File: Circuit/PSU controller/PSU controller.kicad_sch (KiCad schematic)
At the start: 13 parts, among them Q1 S8050

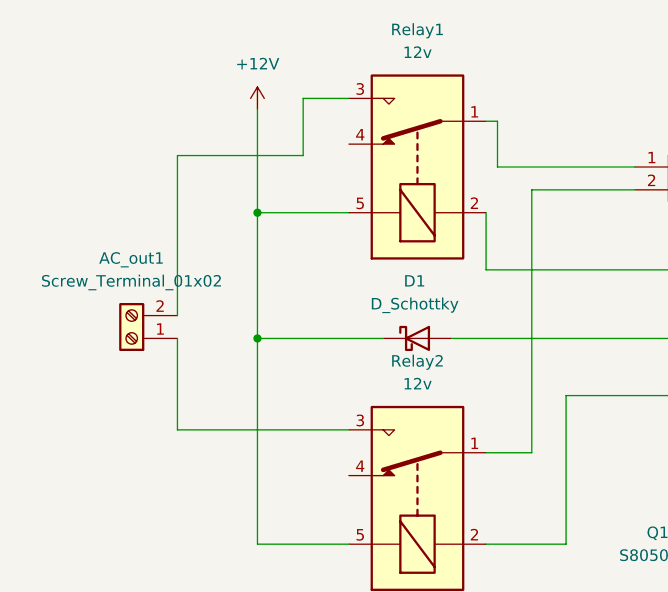
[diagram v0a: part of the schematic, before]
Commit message: Modified PSU controller circuit
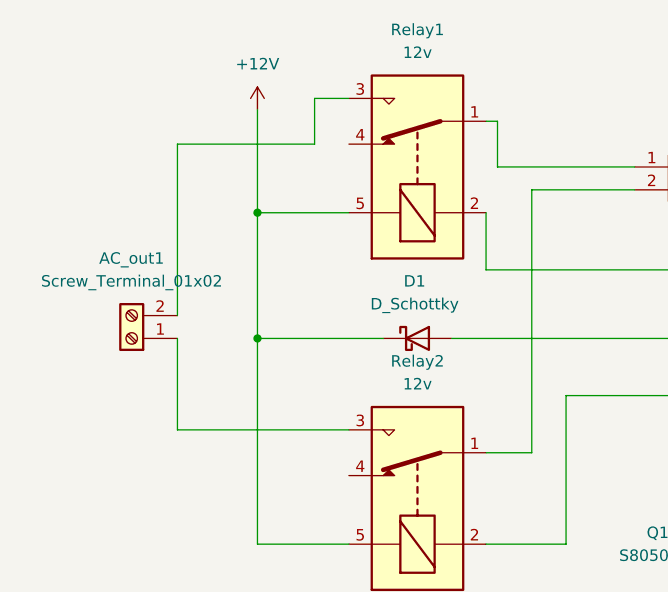
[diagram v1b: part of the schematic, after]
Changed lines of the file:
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@@
+    (stroke (width 0) (type default) (color 0 0 0 0))
+  )
+  (wire (pts (xy 147.32 41.91) (xy 162.56 41.91))
     (stroke (width 0) (type default) (color 0 0 0 0))
   )
@@
     (stroke (width 0) (type default) (color 0 0 0 0))
   )
+  (wire (pts (xy 162.56 36.83) (xy 166.37 36.83))
+    (stroke (width 0) (type default) (color 0 0 0 0))
+  )
   (wire (pts (xy 255.27 74.93) (xy 261.62 74.93))
     (stroke (width 0) (type default) (color 0 0 0 0))
   )
-  (wire (pts (xy 147.32 43.18) (xy 147.32 60.96))
+  (wire (pts (xy 147.32 41.91) (xy 147.32 60.96))
     (stroke (width 0) (type default) (color 0 0 0 0))
   )
@@
     (stroke (width 0) (type default) (color 0 0 0 0))
   )
-  (wire (pts (xy 161.29 36.83) (xy 166.37 36.83))
-    (stroke (width 0) (type default) (color 0 0 0 0))
-  )
   (wire (pts (xy 181.61 55.88) (xy 181.61 49.53))
     (stroke (width 0) (type default) (color 0 0 0 0))
@@
     (stroke (width 0) (type default) (color 0 0 0 0))
   )
+  (wire (pts (xy 147.32 63.5) (xy 147.32 73.66))
+    (stroke (width 0) (type default) (color 0 0 0 0))
+  )
   (wire (pts (xy 156.21 63.5) (xy 170.18 63.5))
     (stroke (width 0) (type default) (color 0 0 0 0))
   )
   (wire (pts (xy 223.52 81.28) (xy 229.87 81.28))
+    (stroke (width 0) (type default) (color 0 0 0 0))
+  )
+  (wire (pts (xy 162.56 41.91) (xy 162.56 36.83))
     (stroke (width 0) (type default) (color 0 0 0 0))
   )
@@
     (stroke (width 0) (type default) (color 0 0 0 0))
   )
-  (wire (pts (xy 147.32 43.18) (xy 161.29 43.18))
+  (wire (pts (xy 147.32 73.66) (xy 166.37 73.66))
     (stroke (width 0) (type default) (color 0 0 0 0))
   )
@@
   )
   (wire (pts (xy 156.21 63.5) (xy 156.21 86.36))
-    (stroke (width 0) (type default) (color 0 0 0 0))
-  )
-  (wire (pts (xy 147.32 73.66) (xy 147.32 63.5))
     (stroke (width 0) (type default) (color 0 0 0 0))
   )
@@
     (stroke (width 0) (type default) (color 0 0 0 0))
   )
-  (wire (pts (xy 161.29 43.18) (xy 161.29 36.83))
-    (stroke (width 0) (type default) (color 0 0 0 0))
-  )
   (wire (pts (xy 218.44 55.88) (xy 223.52 55.88))
     (stroke (width 0) (type default) (color 0 0 0 0))
   )
-  (wire (pts (xy 166.37 73.66) (xy 147.32 73.66))
-    (stroke (width 0) (type default) (color 0 0 0 0))
-  )
